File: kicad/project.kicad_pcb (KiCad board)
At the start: 2 copper layers, 55.9 x 45.7 mm, 1 part, among them U1 ESP32-C3-WROOM-02

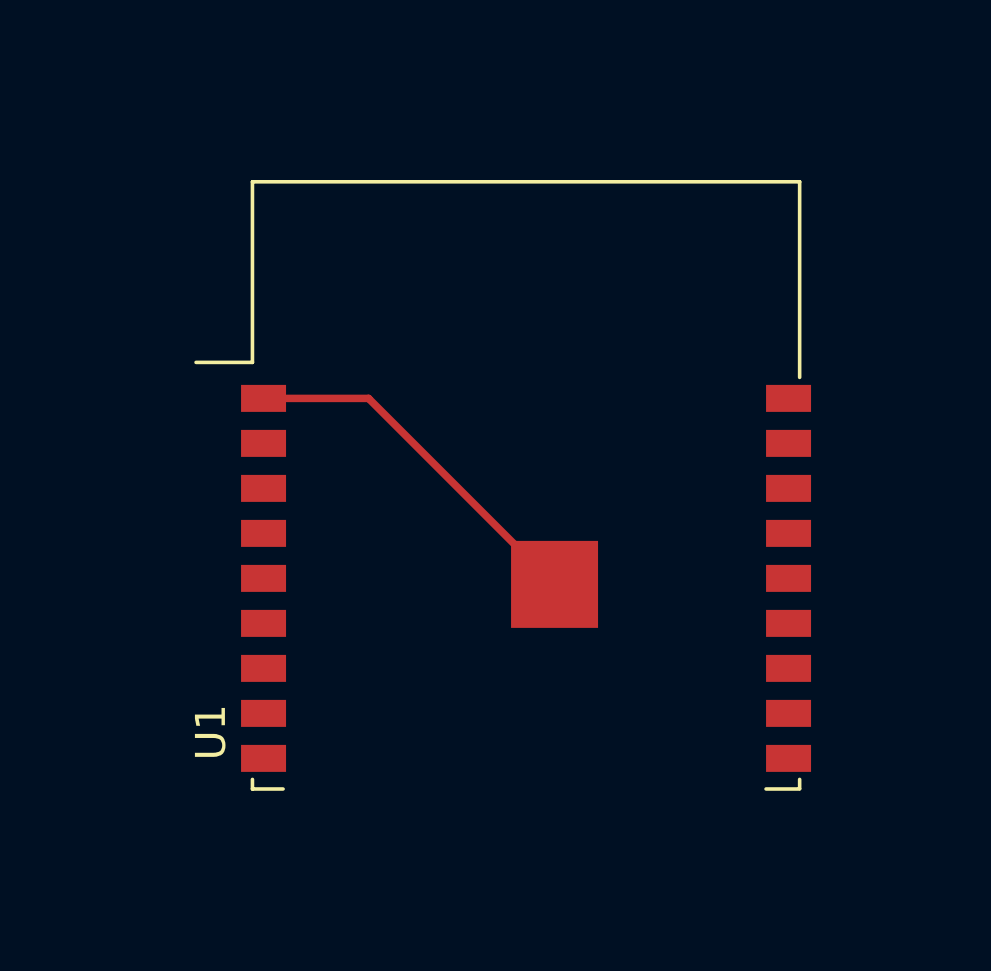
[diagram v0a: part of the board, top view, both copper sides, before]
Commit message: Add partial power management circuit
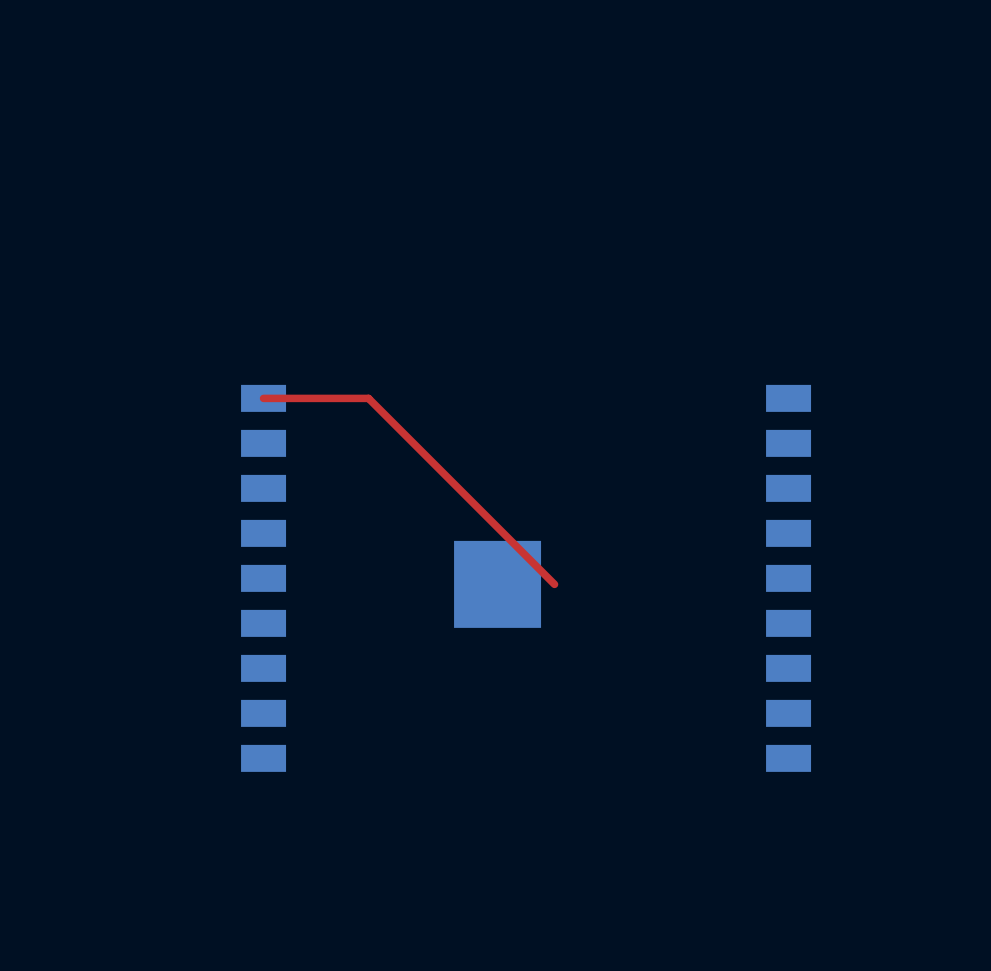
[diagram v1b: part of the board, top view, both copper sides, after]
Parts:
- U1: moved to B.Cu
- turned U1 to 180 degrees

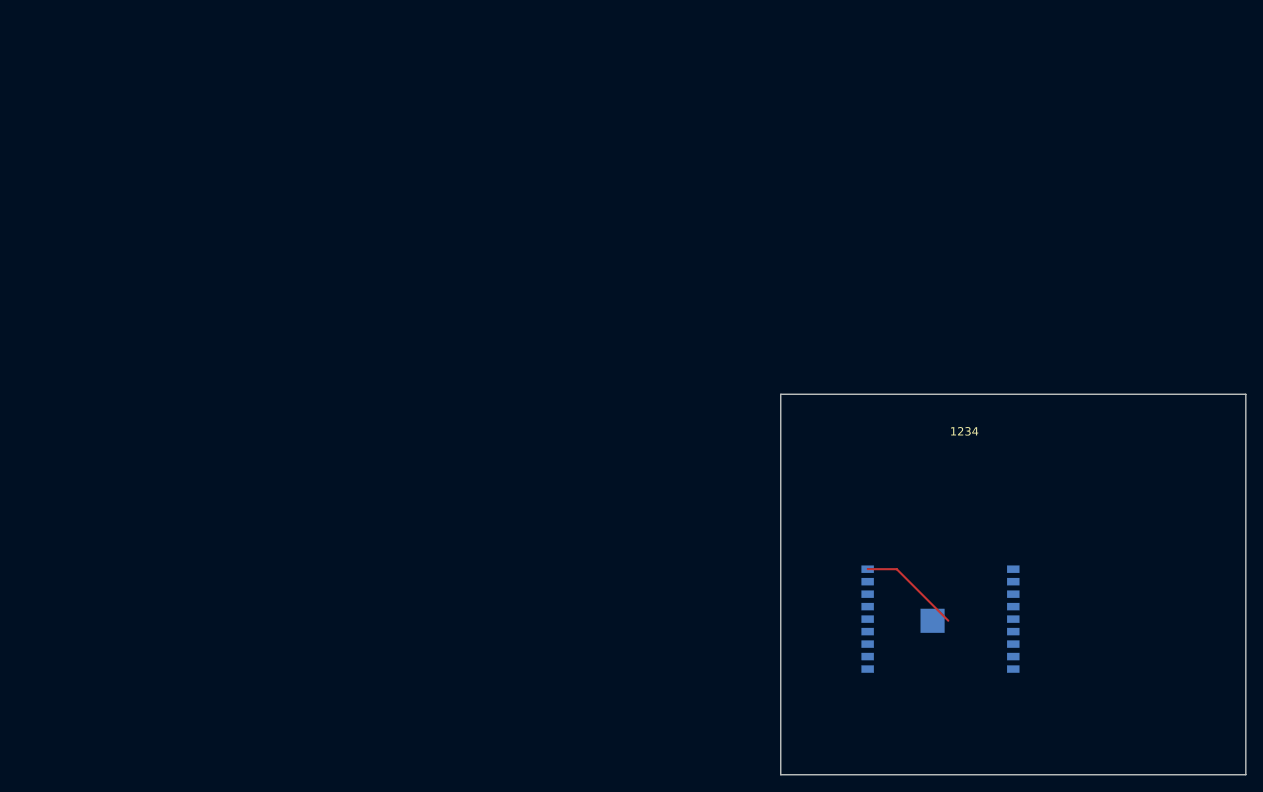
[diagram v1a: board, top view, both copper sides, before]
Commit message: Add USB-C, update power supply, add initial audio components
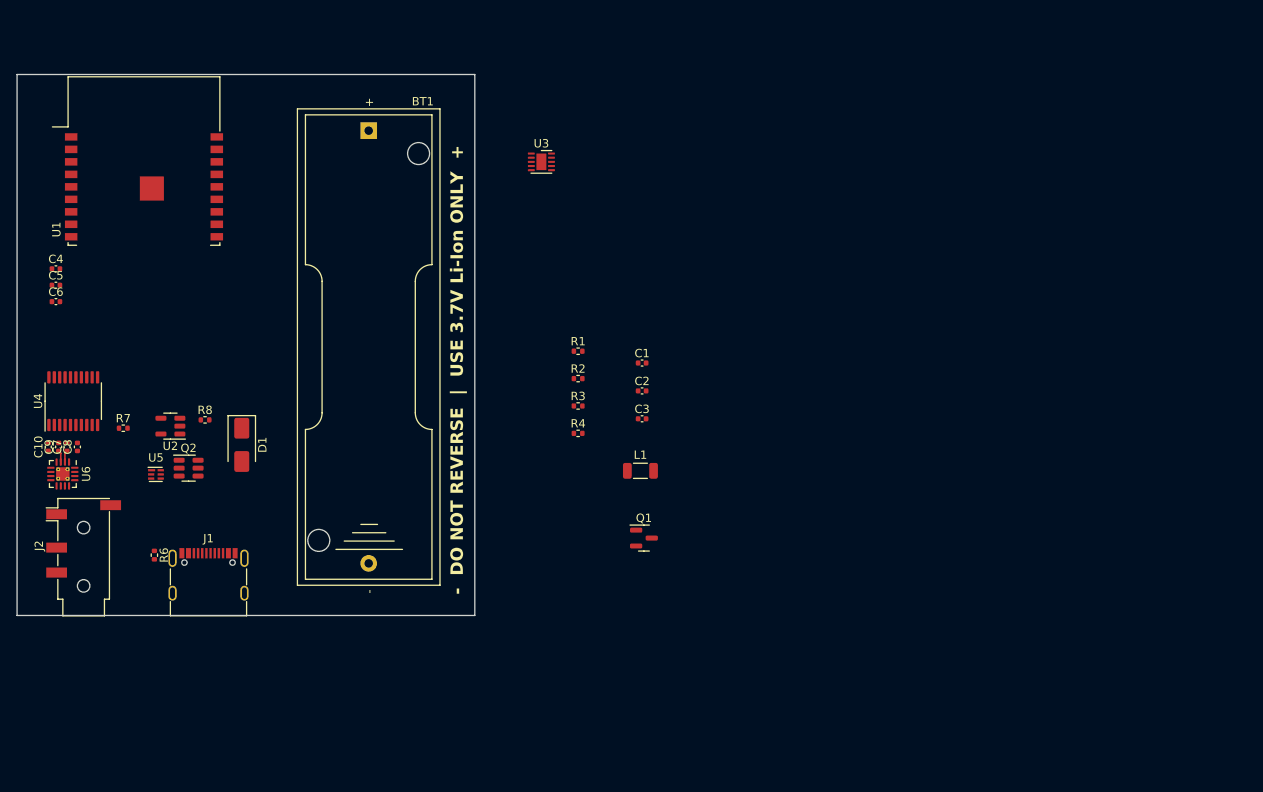
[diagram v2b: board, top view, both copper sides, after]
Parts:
- added BT1: Li-Ion, Battery:BatteryHolder_Keystone_2460_1xAA, F.Cu at (62.2, 26.8)
- added C1: 0.1u, Capacitor_SMD:C_0402_1005Metric, F.Cu at (95.1, 54.7)
- added C10: 1u, Capacitor_SMD:C_0402_1005Metric, F.Cu at (23.8, 64.8)
- added C2: 0.1u, Capacitor_SMD:C_0402_1005Metric, F.Cu at (95.1, 58.0)
- added C3: 10u, Capacitor_SMD:C_0402_1005Metric, F.Cu at (95.1, 61.4)
- added C4: 1u, Capacitor_SMD:C_0402_1005Metric, F.Cu at (24.7, 43.4)
- added C5: 1u, Capacitor_SMD:C_0402_1005Metric, F.Cu at (24.7, 45.3)
- added C6: 1u, Capacitor_SMD:C_0402_1005Metric, F.Cu at (24.7, 47.3)
- added C7: 1u, Capacitor_SMD:C_0402_1005Metric, F.Cu at (26.0, 64.8)
- added C8: 1u, Capacitor_SMD:C_0402_1005Metric, F.Cu at (27.2, 64.8)
- added C9: 1u, Capacitor_SMD:C_0402_1005Metric, F.Cu at (25.0, 64.8)
- added D1: SS54, Diode_SMD:D_SMA, F.Cu at (47.0, 64.5)
- added J1: USB_C_Receptacle_USB2.0, Connector_USB:USB_C_Receptacle_G-Switch_GT-USB-7010ASV, F.Cu at (43.0, 81.2)
- added J2: AudioJack4, Connector_Audio:Jack_3.5mm_PJ320D_Horizontal, F.Cu at (28.0, 76.7)
- added L1: 1.5u, Inductor_SMD:L_1206_3216Metric, F.Cu at (94.9, 67.6)
- added Q1: DMP3165L, Package_TO_SOT_SMD:SOT-23, F.Cu at (95.3, 75.7)
- added Q2: DMG9926UDM, Package_TO_SOT_SMD:SOT-23-6, F.Cu at (40.6, 67.3)
- added R1: 20k, Resistor_SMD:R_0402_1005Metric, F.Cu at (87.4, 53.2)
- added R2: 2k, Resistor_SMD:R_0402_1005Metric, F.Cu at (87.4, 56.5)
- added R3: 2.2k, Resistor_SMD:R_0402_1005Metric, F.Cu at (87.4, 59.8)
- added R4: 330, Resistor_SMD:R_0402_1005Metric, F.Cu at (87.4, 63.1)
- added R6: 1M, Resistor_SMD:R_0402_1005Metric, F.Cu at (36.5, 77.8)
- added R7: 5.1k, Resistor_SMD:R_0402_1005Metric, F.Cu at (32.8, 62.5)
- added R8: 5.1k, Resistor_SMD:R_0402_1005Metric, F.Cu at (42.6, 61.5)
- added U2: MCP73831-2ACI-OT, Package_TO_SOT_SMD:SOT-23-5, F.Cu at (38.4, 62.2)
- added U3: TPS63031DSK, Package_SON:WSON-10-1EP_2.5x2.5mm_P0.5mm_EP1.2x2mm, F.Cu at (83.0, 30.5)
- added U4: PCM5102A, Package_SO:TSSOP-20_4.4x6.5mm_P0.65mm, F.Cu at (26.8, 59.2)
- added U5: BQ29728, Package_SON:WSON-6_1.5x1.5mm_P0.5mm, F.Cu at (36.7, 68.0)
- added U6: PAM8908, Package_DFN_QFN:WQFN-16-1EP_3x3mm_P0.5mm_EP1.6x1.6mm_ThermalVias, F.Cu at (25.5, 68.0)
- U1: moved to F.Cu
- moved U1 108.9 mm to (35.2, 33.5), turned to 0 degrees
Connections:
- U1 pad 1: Net-(U1-GND-Pad1) -> +3V3
- U1 pad 13: unconnected-(U1-D-/IO18-Pad13) -> /D-
- U1 pad 14: unconnected-(U1-D+/IO19-Pad14) -> /D+
- U1 pad 19: Net-(U1-GND-Pad1) -> GND
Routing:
- net Net-(U1-GND-Pad1): track 12.3 -> 0.00 mm
- net /INR+: track 0.00 -> 1.42 mm
- net /INL+: track 0.00 -> 1.42 mm
- added copper zone on In2.Cu, net +3V3
- added copper zone on In1.Cu, net GND
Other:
- board size 55.9 x 45.7 mm -> 55 x 65 mm
- copper layers 2 -> 4
- board text added: "+ DO NOT REVERSE | USE 3.7V Li-Ion ONLY -"
- board text added: "- DO NOT REVERSE | USE 3.7V Li-Ion ONLY +"
- board text removed: "1234"
